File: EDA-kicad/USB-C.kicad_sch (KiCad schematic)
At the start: 3 parts, among them J2 USBC-4-0-CX90MW9-24P1

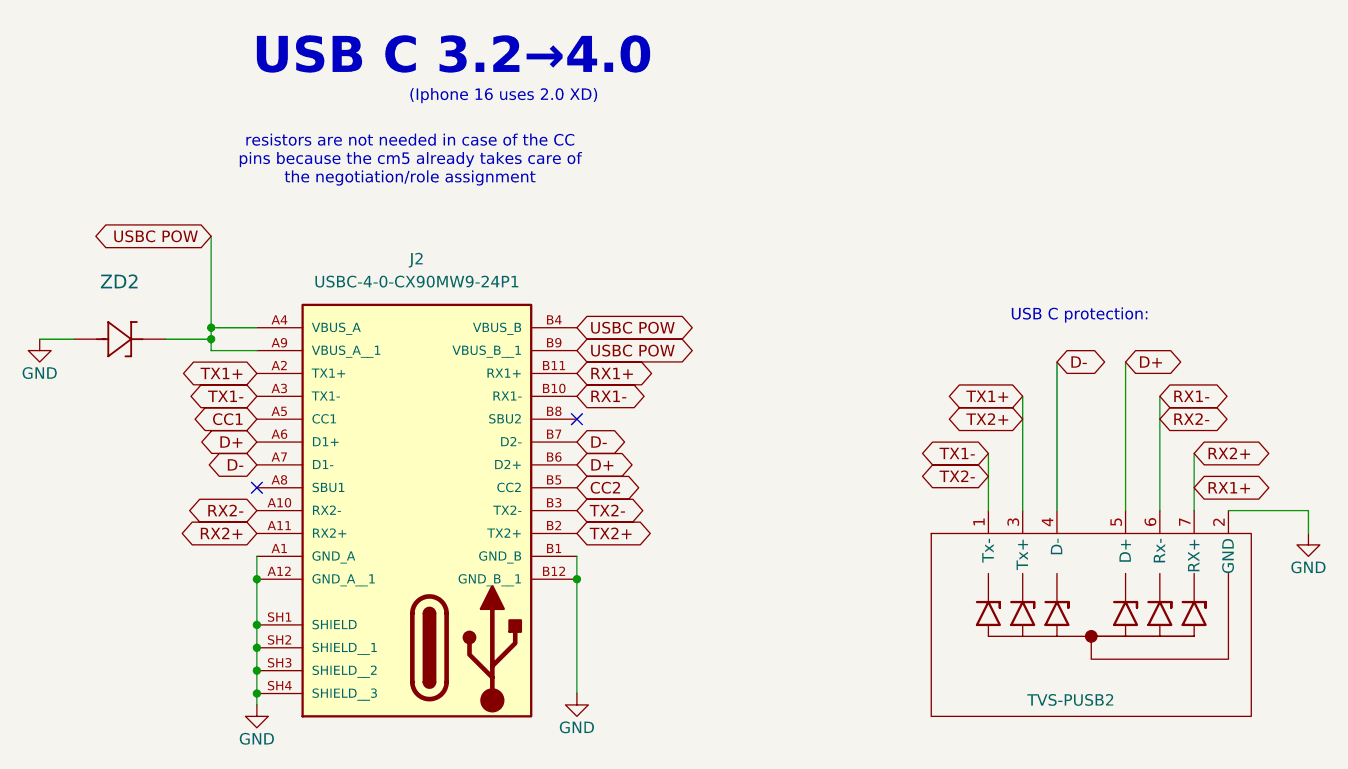
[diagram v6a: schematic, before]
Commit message: reannotate entire schematic
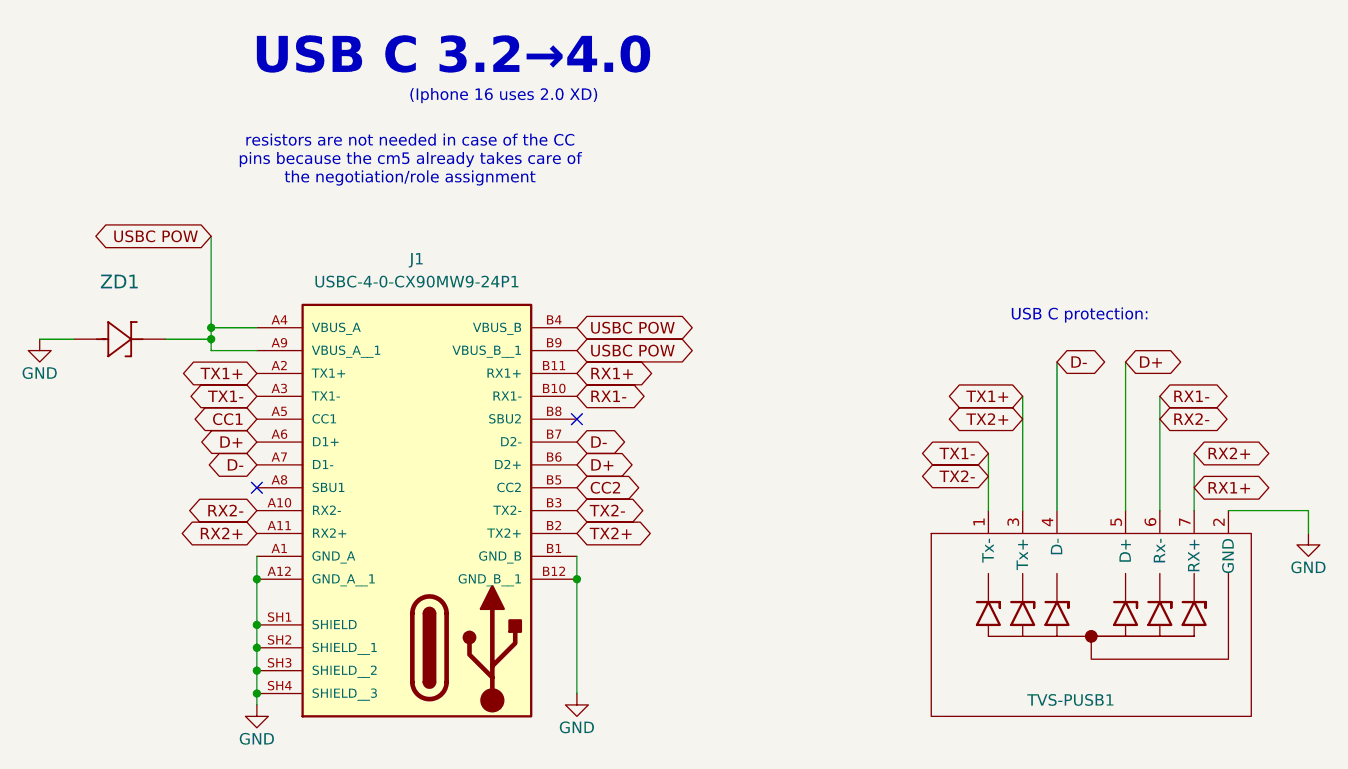
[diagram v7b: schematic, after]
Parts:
- renumbered J2 to J1, TVS-PUSB2 to TVS-PUSB1, ZD2 to ZD1
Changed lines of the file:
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@@
 			"UQAAAGgAAABvAAAAQgAAAG0AAABvAAAATgAAAE0AAAB0AAAAawAAAEQAAABHAAAATAAAAGIAAABi"
 			"AAAARgAAAC8AAABuAAAATAAAAE0AAAByAAAAVwAAADQAAABBAAAANAAAAE8AAABJAAAAQQAAAHcA"
-			"AAA0AAAAcwAAAE8AAABJAAAAdAAAAEYAAAB3AAAAbgAAAFkAAA=="
+			"AAA0AAAAcwAAAE8AAABJAAAAdAAAAEYAAAB3AAAAbgAAAFkAAFYAAAAAAAAAAODS2zne0t5V3tLe"
+			"Vd7S3lXe0t5V4rC/a+90jcTyZH7+8mR+//Jkfv/yZH7/8mR+//Jkfv/yZH7/8mV+0PFjgEgAAAAA"
+			"AAAAAAAAAAAAAAAAAAAAAAAAAADe095W3tPd/wAAAAAAAAAAAAAAAAAAAADe093/3tPeVgAAAAAA"
+			"AAAA3tPd097T3f/e093/3tPd/+O0wv/xaoT/8mR+//Jkfv/yZH7/8mR+//Jkfv/yZH7/8mR+//Jk"
+			"fv/yZH7/8mR+//Jkf5n/ZmYFAAAAAAAAAAAAAAAAAAAAAN7T3lbe093/AAAAAAAAAAAAAAAAAAAA"
+			"AN7T3f/e095WAAAAAAAAAAAAAAAAAAAAAAAAAADyZYBO8mR+/fJkfv/yZH7/8mR+//Jkfv/yZH7/"
+			"8mR+//Jkfv/yZH7/8mR+//Jkfv/yZH7/8mR+//Jkfp4AAAAAAAAAAAAAAAAAAAAA3tPeVt7T3f/e"
+			"1N2q3tTdqt7U3are1N2q3tPd/97T3lYAAAAAAAAAAAAAAAAAAAAA8GKAIvJkfvLyZH7/8mR+//Jk"
+			"fv/yZH7/8mR+//Jkfv/yZH7/8mR+//Jkfv/yZH7/8mR+//Jkfv/yZH7/8mR+//NjfmcAAAAAAAAA"
+			"AAAAAADfz98g3dPdp97U3are1N2q3tTdqt7U3ard092n38/fIAAAAAAAAAAAAAAAAAAAAADxY3+n"
+			"8mR+//Jkfv/yZH7/8mR+//Jkfv/yZH7/8mR+//Jkfv/yZH7/8mR+//Jkfv/yZH7/8mR+//Jkfv/y"
+			"ZH7/8mR+6+5mdw8AAAAAAAAAAAAAAAAAAAAAAAAAAAAAAAAAAAAAAAAAAAAAAAAAAAAAAAAAAAAA"
+			"AAAAAAAA9GR6F/Jkfv3yZH7/8mR+//Jkfv/yZH7/8mR+//Jkfv/yZH7/8mR+//Jkfv/yZH7/8mR+"
+			"//edrf/+8fP/+b3I//Jkfv/yZH7/82R+aQAAAAAAAAAAAAAAAAAAAAAAAAAAAAAAAAAAAAAAAAAA"
+			"AAAAAAAAAAAAAAAAAAAAAAAAAADyY31k8mR+//Jkfv/yZH7/8mR+//Jkfv/yZH7/8mR+//Jkfv/y"
+			"ZH7/8mR+//Jkfv/3nq////7+///////+9fb/8mR+//Jkfv/yZH23AAAAAAAAAADfz98g3dPdp97U"
+			"3are1N2q3tTdqt7U3ard092n38/fIAAAAAAAAAAAAAAAAPJlfo7yZH7/8mR+//JmgP/4qLf/9pmr"
+			"//Jkfv/yZH7/8mR+//Jkfv/yZH7/956v///+/v////////7+//ehsf/yZH7/8mR+//NkfuEAAAAA"
+			"AAAAAN7T3lbe093/3tTdqt7U3are1N2q3tTdqt7T3f/e095WAA=="
 		)
 	)
@@
 		(on_board yes)
 		(dnp no)
-		(property "Reference" "#PWR082"
+		(property "Reference" "#PWR051"
 			(at 214.63 119.38 0)
 			(effects
@@
 			(project "cm5-carrier"
 				(path "/28c5e4fe-1ec7-4477-97f0-d2ec1401fad5/4d20c3c8-7f3b-4711-a43f-15c2a08af985"
-					(reference "#PWR082")
+					(reference "#PWR051")
 					(unit 1)
 				)
@@
 		(on_board yes)
 		(dnp no)
-		(property "Reference" "#PWR080"
+		(property "Reference" "#PWR053"
 			(at 97.79 138.43 0)
 			(effects
@@
 			(project "cm5-carrier"
 				(path "/28c5e4fe-1ec7-4477-97f0-d2ec1401fad5/4d20c3c8-7f3b-4711-a43f-15c2a08af985"
-					(reference "#PWR080")
+					(reference "#PWR053")
 					(unit 1)
 				)
@@
 		(dnp no)
 		(fields_autoplaced yes)
-		(property "Reference" "ZD2"
+		(property "Reference" "ZD1"
 			(at 82.55 85.09 0)
 			(effects
@@
 			(project "cm5-carrier"
 				(path "/28c5e4fe-1ec7-4477-97f0-d2ec1401fad5/4d20c3c8-7f3b-4711-a43f-15c2a08af985"
-					(reference "ZD2")
+					(reference "ZD1")
 					(unit 1)
 				)
@@
 		(on_board yes)
 		(dnp no)
-		(property "Reference" "#PWR079"
+		(property "Reference" "#PWR050"
 			(at 73.66 97.79 0)
 			(effects
@@
 			(project "cm5-carrier"
 				(path "/28c5e4fe-1ec7-4477-97f0-d2ec1401fad5/4d20c3c8-7f3b-4711-a43f-15c2a08af985"
-					(reference "#PWR079")
+					(reference "#PWR050")
 					(unit 1)
 				)
@@
 		(on_board yes)
 		(dnp no)
-		(property "Reference" "#PWR081"
+		(property "Reference" "#PWR052"
 			(at 133.35 137.16 0)
 			(effects
@@
 			(project "cm5-carrier"
 				(path "/28c5e4fe-1ec7-4477-97f0-d2ec1401fad5/4d20c3c8-7f3b-4711-a43f-15c2a08af985"
-					(reference "#PWR081")
+					(reference "#PWR052")
 					(unit 1)
 				)
@@
 		(on_board yes)
 		(dnp no)
-		(property "Reference" "TVS-PUSB2"
+		(property "Reference" "TVS-PUSB1"
 			(at 183.388 131.572 0)
 			(effects
@@
 			(project "cm5-carrier"
 				(path "/28c5e4fe-1ec7-4477-97f0-d2ec1401fad5/4d20c3c8-7f3b-4711-a43f-15c2a08af985"
-					(reference "TVS-PUSB2")
+					(reference "TVS-PUSB1")
 					(unit 1)
 				)
@@
 		(dnp no)
 		(fields_autoplaced yes)
-		(property "Reference" "J2"
+		(property "Reference" "J1"
 			(at 115.57 82.55 0)
 			(effects
@@
 			(project ""
 				(path "/28c5e4fe-1ec7-4477-97f0-d2ec1401fad5/4d20c3c8-7f3b-4711-a43f-15c2a08af985"
-					(reference "J2")
+					(reference "J1")
 					(unit 1)
 				)
